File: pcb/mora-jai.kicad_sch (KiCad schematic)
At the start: 32 parts, among them J2 Conn_01x04, J5 Conn_01x03, SW1 SW_Push, SW10 SW_Push, SW11 SW_Push, SW12 SW_Push, SW13 SW_Push, SW14 SW_Push, SW15 SW_Push, SW16 SW_Push, SW2 SW_Push, SW3 SW_Push, SW4 SW_Push, SW5 SW_Push, SW6 SW_Push, SW7 SW_Push, SW8 SW_Push, SW9 SW_Push, U1 CD74HC4067M, U3 XIAO-ESP32-S3-SMD

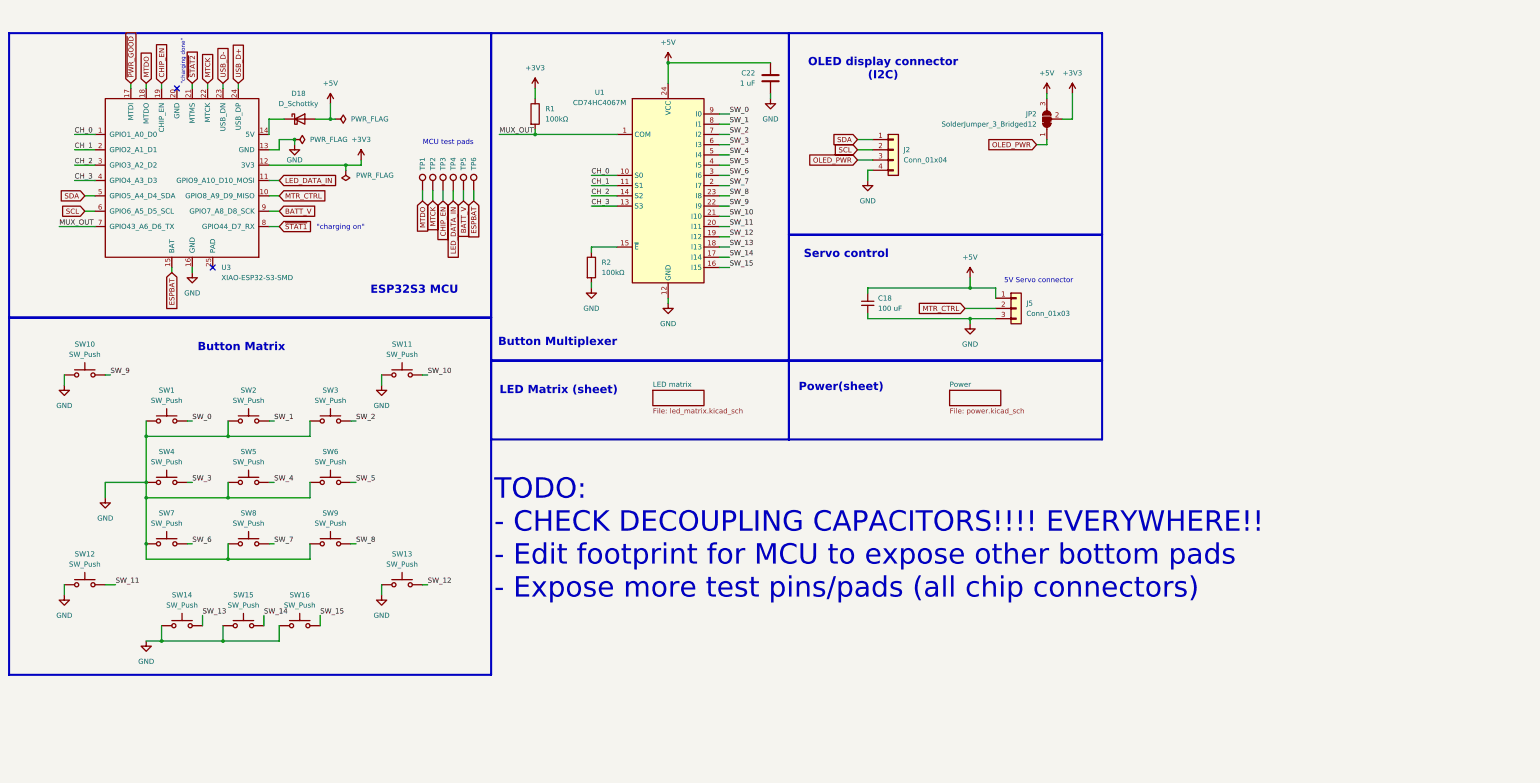
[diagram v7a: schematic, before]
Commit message: drew fill zones for 5V boost circuit
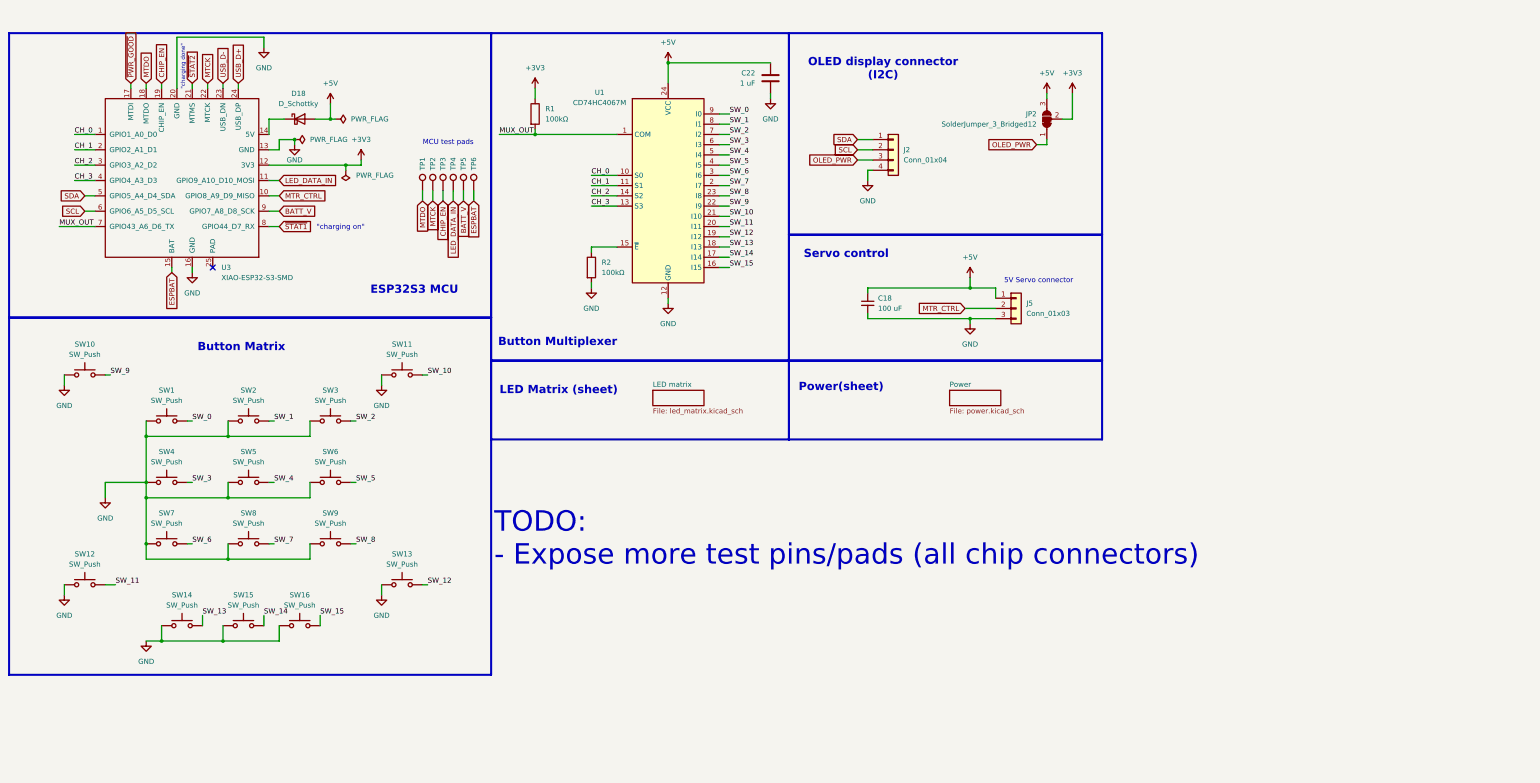
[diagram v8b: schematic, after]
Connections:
- net GND: now also U3.20 (GND)
- no-connect marks 2 -> 1
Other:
- note added: "TODO: - Expose more test pins/pads (all chip connectors)"
- note removed: "TODO: - CHECK DECOUPLING CAPACITORS!!!! EVERYWHERE!! - Edit footprint for MCU to expose other bottom pads - Expose more test pins/pads (all chip connectors)"
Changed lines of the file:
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@@
 		)
 	)
-	(text "TODO:\n- CHECK DECOUPLING CAPACITORS!!!! EVERYWHERE!!\n- Edit footprint for MCU to expose other bottom pads\n- Expose more test pins/pads (all chip connectors)\n"
+	(text "TODO:\n- Expose more test pins/pads (all chip connectors)\n"
 		(exclude_from_sim no)
 		(at 133.35 138.43 0)
@@
 	(text "\"charging done\""
 		(exclude_from_sim no)
-		(at 56.134 20.066 90)
+		(at 56.134 21.336 90)
 		(effects
 			(font
@@
 	)
 	(no_connect
-		(at 54.61 26.67)
-	)
-	(no_connect
 		(at 63.5 71.12)
 	)
@@
 	(wire
 		(pts
+			(xy 54.61 26.67) (xy 54.61 13.97)
+		)
+		(stroke
+			(width 0)
+			(type default)
+		)
+	)
+	(wire
+		(pts
 			(xy 143.51 26.67) (xy 143.51 29.21)
 		)
@@
 	(wire
 		(pts
+			(xy 76.2 13.97) (xy 76.2 16.51)
+		)
+		(stroke
+			(width 0)
+			(type default)
+		)
+	)
+	(wire
+		(pts
 			(xy 80.01 163.83) (xy 66.04 163.83)
 		)
@@
 	(wire
 		(pts
+			(xy 54.61 13.97) (xy 76.2 13.97)
+		)
+		(stroke
+			(width 0)
+			(type default)
+		)
+	)
+	(wire
+		(pts
 			(xy 223.52 41.91) (xy 227.33 41.91)
 		)
@@
 					(unit 1)
 				)
+			)
+		)
+	)
+	(symbol
+		(lib_id "power:GND")
+		(at 76.2 16.51 0)
+		(unit 1)
+		(body_style 1)
+		(exclude_from_sim no)
+		(in_bom yes)
+		(on_board yes)
+		(in_pos_files yes)
+		(dnp no)
+		(fields_autoplaced yes)
+		(property "Reference" "#PWR056"
+			(at 76.2 22.86 0)
+			(hide yes)
+			(show_name no)
+			(do_not_autoplace no)
+			(effects
+				(font
+					(size 1.27 1.27)
+				)
+			)
+		)
+		(property "Value" "GND"
+			(at 76.2 21.59 0)
+			(show_name no)
+			(do_not_autoplace no)
+			(effects
+				(font
+					(size 1.27 1.27)
+				)
+			)
+		)
+		(property "Footprint" ""
+			(at 76.2 16.51 0)
+			(hide yes)
+			(show_name no)
+			(do_not_autoplace no)
+			(effects
+				(font
+					(size 1.27 1.27)
+				)
+			)
+		)
+		(property "Datasheet" ""
+			(at 76.2 16.51 0)
+			(hide yes)
+			(show_name no)
+			(do_not_autoplace no)
+			(effects
+				(font
+					(size 1.27 1.27)
+				)
+			)
+		)
+		(property "Description" "Power symbol creates a global label with name \"GND\" , ground"
+			(at 76.2 16.51 0)
+			(hide yes)
+			(show_name no)
+			(do_not_autoplace no)
+			(effects
+				(font
+					(size 1.27 1.27)
+				)
+			)
+		)
+		(pin "1"
+		)
+		(instances
+			(project "mora-jai"
+				(path "/06a165cb-987d-4515-950b-4b68772ab4b3"
+					(reference "#PWR056")
+					(unit 1)
+				)
